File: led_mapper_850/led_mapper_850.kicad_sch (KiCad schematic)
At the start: 530 parts, among them J1 Conn_02x12_Top_Bottom

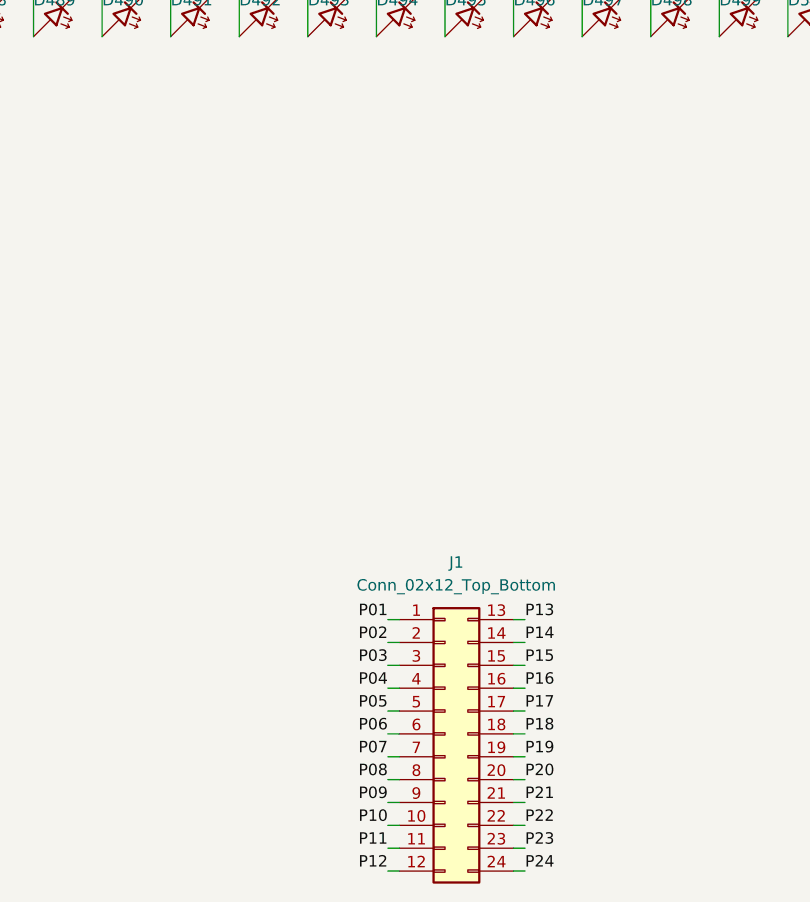
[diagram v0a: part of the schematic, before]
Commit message: lay out network from pcb positions
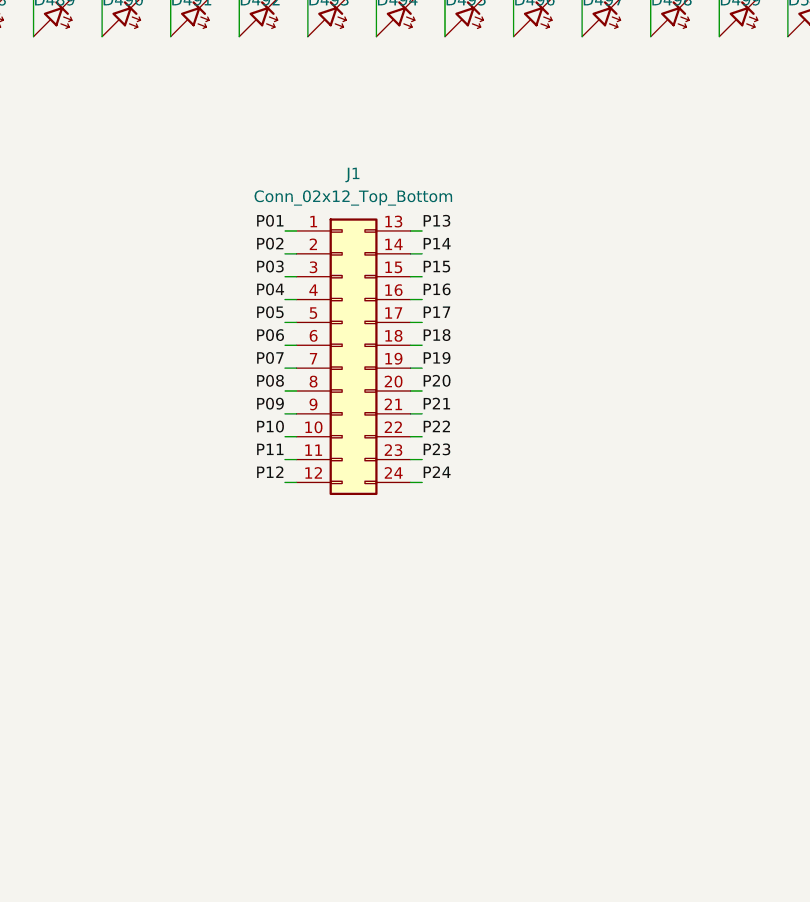
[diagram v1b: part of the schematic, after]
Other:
- moved on the sheet: J1
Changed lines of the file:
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@@
 	(wire
 		(pts
-			(xy 299.72 198.12) (xy 300.99 198.12)
+			(xy 288.29 154.94) (xy 289.56 154.94)
 		)
 		(stroke
@@
 	(wire
 		(pts
-			(xy 314.96 175.26) (xy 313.69 175.26)
+			(xy 303.53 132.08) (xy 302.26 132.08)
 		)
 		(stroke
@@
 	(wire
 		(pts
-			(xy 299.72 172.72) (xy 300.99 172.72)
+			(xy 288.29 129.54) (xy 289.56 129.54)
 		)
 		(stroke
@@
 	(wire
 		(pts
-			(xy 299.72 200.66) (xy 300.99 200.66)
+			(xy 288.29 157.48) (xy 289.56 157.48)
 		)
 		(stroke
@@
 	(wire
 		(pts
-			(xy 314.96 198.12) (xy 313.69 198.12)
+			(xy 303.53 154.94) (xy 302.26 154.94)
 		)
 		(stroke
@@
 	(wire
 		(pts
-			(xy 299.72 185.42) (xy 300.99 185.42)
+			(xy 288.29 142.24) (xy 289.56 142.24)
 		)
 		(stroke
@@
 	(wire
 		(pts
-			(xy 314.96 195.58) (xy 313.69 195.58)
+			(xy 303.53 152.4) (xy 302.26 152.4)
 		)
 		(stroke
@@
 	(wire
 		(pts
-			(xy 314.96 180.34) (xy 313.69 180.34)
+			(xy 303.53 137.16) (xy 302.26 137.16)
 		)
 		(stroke
@@
 	(wire
 		(pts
-			(xy 314.96 182.88) (xy 313.69 182.88)
+			(xy 303.53 139.7) (xy 302.26 139.7)
 		)
 		(stroke
@@
 	(wire
 		(pts
-			(xy 314.96 177.8) (xy 313.69 177.8)
+			(xy 303.53 134.62) (xy 302.26 134.62)
 		)
 		(stroke
@@
 	(wire
 		(pts
-			(xy 314.96 185.42) (xy 313.69 185.42)
+			(xy 303.53 142.24) (xy 302.26 142.24)
 		)
 		(stroke
@@
 	(wire
 		(pts
-			(xy 314.96 187.96) (xy 313.69 187.96)
+			(xy 303.53 144.78) (xy 302.26 144.78)
 		)
 		(stroke
@@
 	(wire
 		(pts
-			(xy 299.72 187.96) (xy 300.99 187.96)
+			(xy 288.29 144.78) (xy 289.56 144.78)
 		)
 		(stroke
@@
 	(wire
 		(pts
-			(xy 299.72 193.04) (xy 300.99 193.04)
+			(xy 288.29 149.86) (xy 289.56 149.86)
 		)
 		(stroke
@@
 	(wire
 		(pts
-			(xy 314.96 190.5) (xy 313.69 190.5)
+			(xy 303.53 147.32) (xy 302.26 147.32)
 		)
 		(stroke
@@
 	(wire
 		(pts
-			(xy 299.72 182.88) (xy 300.99 182.88)
+			(xy 288.29 139.7) (xy 289.56 139.7)
 		)
 		(stroke
@@
 	(wire
 		(pts
-			(xy 314.96 200.66) (xy 313.69 200.66)
+			(xy 303.53 157.48) (xy 302.26 157.48)
 		)
 		(stroke
@@
 	(wire
 		(pts
-			(xy 314.96 172.72) (xy 313.69 172.72)
+			(xy 303.53 129.54) (xy 302.26 129.54)
 		)
 		(stroke
@@
 	(wire
 		(pts
-			(xy 299.72 175.26) (xy 300.99 175.26)
+			(xy 288.29 132.08) (xy 289.56 132.08)
 		)
 		(stroke
@@
 	(wire
 		(pts
-			(xy 299.72 177.8) (xy 300.99 177.8)
+			(xy 288.29 134.62) (xy 289.56 134.62)
 		)
 		(stroke
@@
 	(wire
 		(pts
-			(xy 299.72 195.58) (xy 300.99 195.58)
+			(xy 288.29 152.4) (xy 289.56 152.4)
 		)
 		(stroke
@@
 	(wire
 		(pts
-			(xy 299.72 190.5) (xy 300.99 190.5)
+			(xy 288.29 147.32) (xy 289.56 147.32)
 		)
 		(stroke
@@
 	(wire
 		(pts
-			(xy 314.96 193.04) (xy 313.69 193.04)
+			(xy 303.53 149.86) (xy 302.26 149.86)
 		)
 		(stroke
@@
 	(wire
 		(pts
-			(xy 299.72 180.34) (xy 300.99 180.34)
+			(xy 288.29 137.16) (xy 289.56 137.16)
 		)
 		(stroke
@@
 	)
 	(label "P20"
-		(at 314.96 190.5 0)
+		(at 303.53 147.32 0)
 		(effects
 			(font
@@
 	)
 	(label "P14"
-		(at 314.96 175.26 0)
+		(at 303.53 132.08 0)
 		(effects
 			(font
@@
 	)
 	(label "P18"
-		(at 314.96 185.42 0)
+		(at 303.53 142.24 0)
 		(effects
 			(font
@@
 	)
 	(label "P11"
-		(at 299.72 198.12 180)
+		(at 288.29 154.94 180)
 		(effects
 			(font
@@
 	)
 	(label "P17"
-		(at 314.96 182.88 0)
+		(at 303.53 139.7 0)
 		(effects
 			(font
@@
 	)
 	(label "P05"
-		(at 299.72 182.88 180)
+		(at 288.29 139.7 180)
 		(effects
 			(font
@@
 	)
 	(label "P07"
-		(at 299.72 187.96 180)
+		(at 288.29 144.78 180)
 		(effects
 			(font
@@
 	)
 	(label "P02"
-		(at 299.72 175.26 180)
+		(at 288.29 132.08 180)
 		(effects
 			(font
@@
 	)
 	(label "P21"
-		(at 314.96 193.04 0)
+		(at 303.53 149.86 0)
 		(effects
 			(font
@@
 	)
 	(label "P09"
-		(at 299.72 193.04 180)
+		(at 288.29 149.86 180)
 		(effects
 			(font
@@
 	)
 	(label "P08"
-		(at 299.72 190.5 180)
+		(at 288.29 147.32 180)
 		(effects
 			(font
@@
 	)
 	(label "P13"
-		(at 314.96 172.72 0)
+		(at 303.53 129.54 0)
 		(effects
 			(font
@@
 	)
 	(label "P23"
-		(at 314.96 198.12 0)
+		(at 303.53 154.94 0)
 		(effects
 			(font
@@
 	)
 	(label "P10"
-		(at 299.72 195.58 180)
+		(at 288.29 152.4 180)
 		(effects
 			(font
@@
 	)
 	(label "P16"
-		(at 314.96 180.34 0)
+		(at 303.53 137.16 0)
 		(effects
 			(font
@@
 	)
 	(label "P15"
-		(at 314.96 177.8 0)
+		(at 303.53 134.62 0)
 		(effects
 			(font
@@
 	)
 	(label "P06"
-		(at 299.72 185.42 180)
+		(at 288.29 142.24 180)
 		(effects
 			(font
@@
 	)
 	(label "P12"
-		(at 299.72 200.66 180)
+		(at 288.29 157.48 180)
 		(effects
 			(font
@@
 	)
 	(label "P01"
-		(at 299.72 172.72 180)
+		(at 288.29 129.54 180)
 		(effects
 			(font
@@
 	)
 	(label "P24"
-		(at 314.96 200.66 0)
+		(at 303.53 157.48 0)
 		(effects
 			(font
@@
 	)
 	(label "P04"
-		(at 299.72 180.34 180)
+		(at 288.29 137.16 180)
 		(effects
 			(font
@@
 	)
 	(label "P19"
-		(at 314.96 187.96 0)
+		(at 303.53 144.78 0)
 		(effects
 			(font
@@
 	)
 	(label "P03"
-		(at 299.72 177.8 180)
+		(at 288.29 134.62 180)
 		(effects
 			(font
@@
 	)
 	(label "P22"
-		(at 314.96 195.58 0)
+		(at 303.53 152.4 0)
 		(effects
 			(font
@@
 	(symbol
 		(lib_id "Connector_Generic:Conn_02x12_Top_Bottom")
-		(at 306.07 185.42 0)
+		(at 294.64 142.24 0)
 		(unit 1)
 		(exclude_from_sim no)
@@
 		(fields_autoplaced yes)
 		(property "Reference" "J1"
-			(at 307.34 166.37 0)
+			(at 295.91 123.19 0)
 			(effects
 				(font
@@
 		)
 		(property "Value" "Conn_02x12_Top_Bottom"
-			(at 307.34 168.91 0)
+			(at 295.91 125.73 0)
 			(effects
 				(font
@@
 		)
 		(property "Footprint" "ccatlib:PinSocket_2x12_P2.54mm_Vertical_SMD_custom"
-			(at 306.07 185.42 0)
+			(at 294.64 142.24 0)
 			(effects
 				(font
@@
 		)
 		(property "Datasheet" "~"
-			(at 306.07 185.42 0)
+			(at 294.64 142.24 0)
 			(effects
 				(font
@@
 		)
 		(property "Description" "Generic connector, double row, 02x12, top/bottom pin numbering scheme (row 1: 1...pins_per_row, row2: pins_per_row+1 ... num_pins), script generated (kicad-library-utils/schlib/autogen/connector/)"
-			(at 306.07 185.42 0)
+			(at 294.64 142.24 0)
 			(effects
 				(font

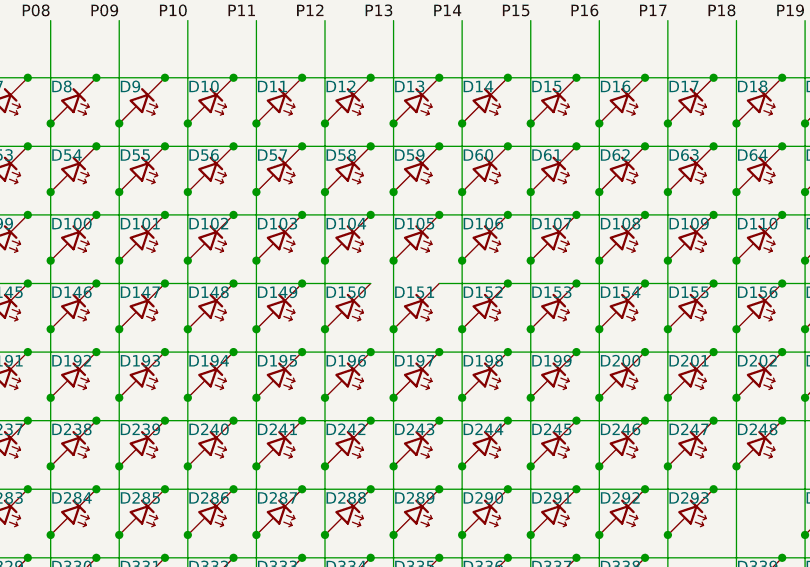
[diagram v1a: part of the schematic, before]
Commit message: fix wire disconnect
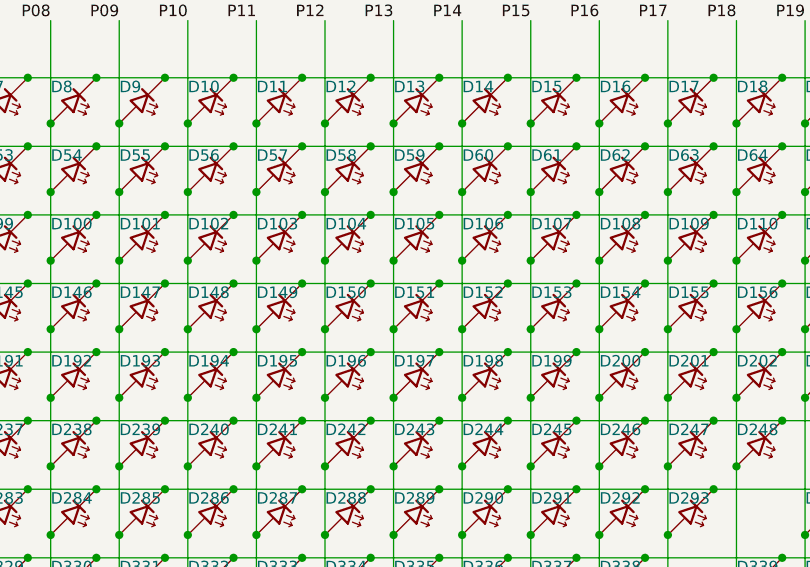
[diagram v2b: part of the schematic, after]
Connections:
- net P21: now also D151.1 (K), D152.1 (K), D153.1 (K), D154.1 (K), D155.1 (K), D156.1 (K), D157.1 (K), D158.1 (K), D159.1 (K), D160.1 (K), D161.1 (K)
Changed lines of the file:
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@@
 	)
 	(junction
+		(at 113.03 49.53)
+		(diameter 0)
+		(color 0 0 0 0)
+	)
+	(junction
 		(at 364.49 49.53)
 		(diameter 0)
@@
 	)
 	(junction
+		(at 120.65 49.53)
+		(diameter 0)
+		(color 0 0 0 0)
+	)
+	(junction
 		(at 237.49 100.33)
 		(diameter 0)
@@
 		)
 		(stroke
+			(width 0)
+			(type default)
+		)
+	)
+	(wire
+		(pts
+			(xy 113.03 49.53) (xy 120.65 49.53)
+		)
+		(stroke

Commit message: split into four networks
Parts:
- removed D1, D10, D100, D101, D102, D103, D104, D105, D106, D107, D108, D109, D11, D110, D111, D112, D113, D114, D115, D116, D117, D118, D119, D12, D120, D121, D122, D123, D124, D125, D126, D127, D128, D129, D13, D130, D131, D132, D133, D134, D135, D136, D137, D138, D139, D14, D140, D141, D142, D143, D144, D145, D146, D147, D148, D149, D15, D150, D151, D152, D153, D154, D155, D156, D157, D158, D159, D16, D160, D161, D162, D163, D164, D165, D166, D167, D168, D169, D17, D170, D171, D172, D173, D174, D175, D176, D177, D178, D179, D18, D180, D181, D182, D183, D184, D185, D186, D187, D188, D189, D19, D190, D191, D192, D193, D194, D195, D196, D197, D198, D199, D2, D20, D200, D201, D202, D203, D204, D205, D206, D207, D208, D209, D21, D210, D211, D212, D213, D214, D215, D216, D217, D218, D219, D22, D220, D221, D222, D223, D224, D225, D226, D227, D228, D229, D23, D230, D231, D232, D233, D234, D235, D236, D237, D238, D239, D24, D240, D241, D242, D243, D244, D245, D246, D247, D248, D249, D25, D250, D251, D252, D253, D254, D255, D256, D257, D258, D259, D26, D260, D261, D262, D263, D264, D265, D266, D267, D268, D269, D27, D270, D271, D272, D273, D274, D275, D276, D277, D278, D279, D28, D280, D281, D282, D283, D284, D285, D286, D287, D288, D289, D29, D290, D291, D292, D293, D294, D295, D296, D297, D298, D299, D3, D30, D300, D301, D302, D303, D304, D305, D306, D307, D308, D309, D31, D310, D311, D312, D313, D314, D315, D316, D317, D318, D319, D32, D320, D321, D322, D323, D324, D325, D326, D327, D328, D329, D33, D330, D331, D332, D333, D334, D335, D336, D337, D338, D339, D34, D340, D341, D342, D343, D344, D345, D346, D347, D348, D349, D35, D350, D351, D352, D353, D354, D355, D356, D357, D358, D359, D36, D360, D361, D362, D363, D364, D365, D366, D367, D368, D369, D37, D370, D371, D372, D373, D374, D375, D376, D377, D378, D379, D38, D380, D381, D382, D383, D384, D385, D386, D387, D388, D389, D39, D390, D391, D392, D393, D394, D395, D396, D397, D398, D399, D4, D40, D400, D401, D402, D403, D404, D405, D406, D407, D408, D409, D41, D410, D411, D412, D413, D414, D415, D416, D417, D418, D419, D42, D420, D421, D422, D423, D424, D425, D426, D427, D428, D429, D43, D430, D431, D432, D433, D434, D435, D436, D437, D438, D439, D44, D440, D441, D442, D443, D444, D445, D446, D447, D448, D449, D45, D450, D451, D452, D453, D454, D455, D456, D457, D458, D459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: LED, LED_SMD:LED_0201_0603Metric, symbol Device:LED_45deg
- removed J1: Conn_02x12_Top_Bottom, ccatlib:PinSocket_2x12_P2.54mm_Vertical_SMD_custom, symbol Connector_Generic:Conn_02x12_Top_Bottom
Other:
- added sheet network1 (untitled.kicad_sch)
- added sheet network2 (untitled.kicad_sch)
- added sheet network3 (untitled.kicad_sch)
- added sheet network4 (untitled.kicad_sch)

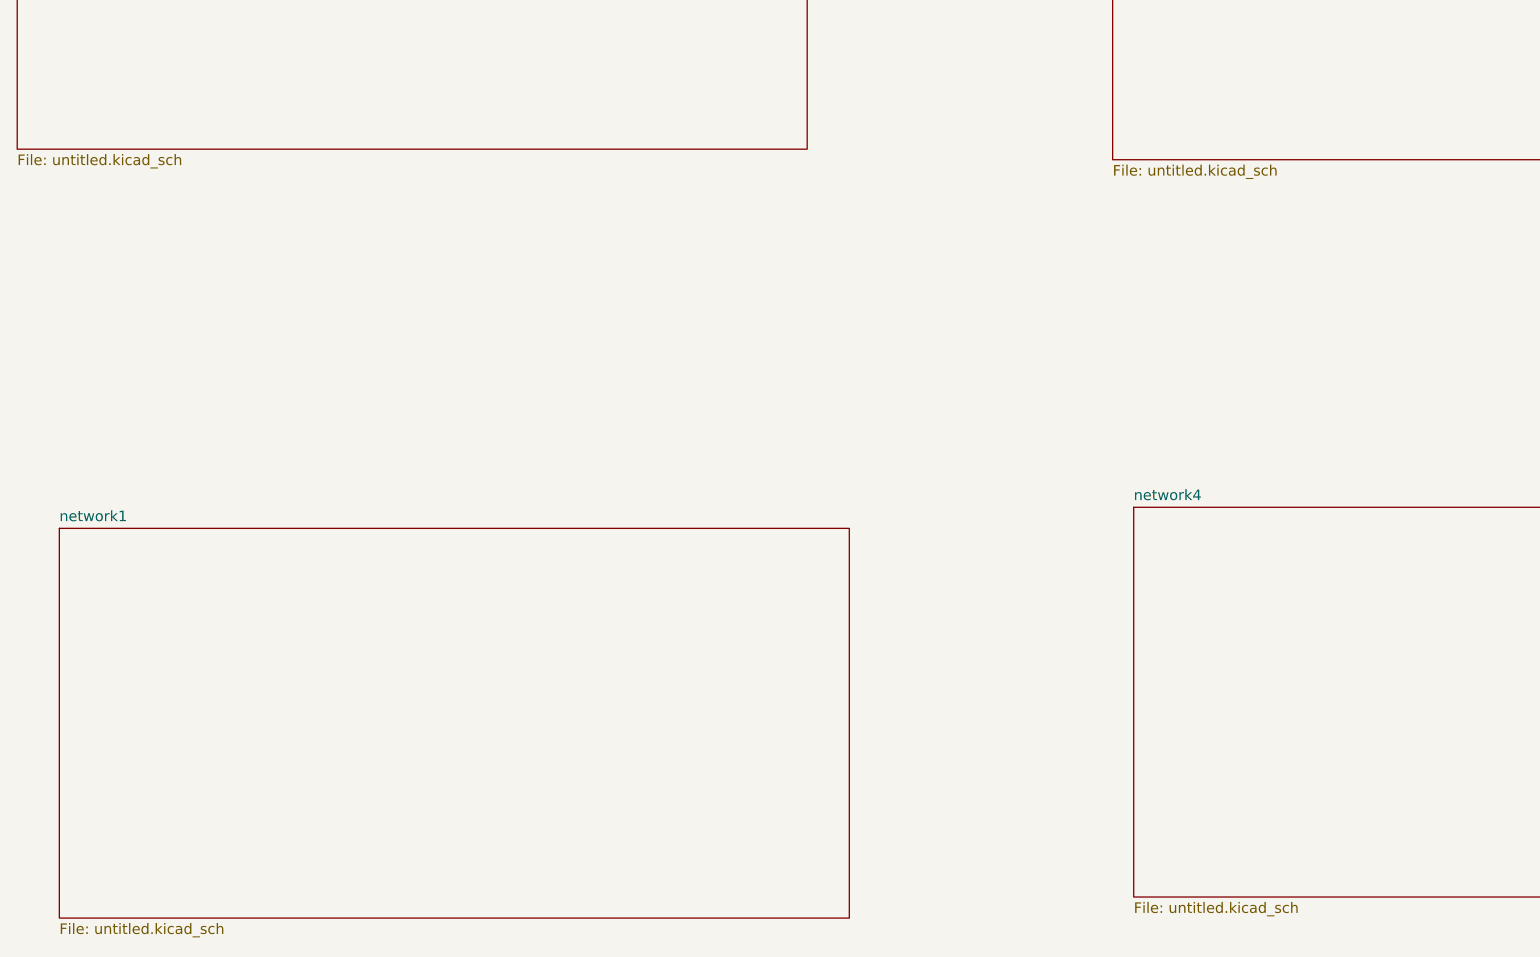
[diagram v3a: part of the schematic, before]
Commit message: rename single net schematic
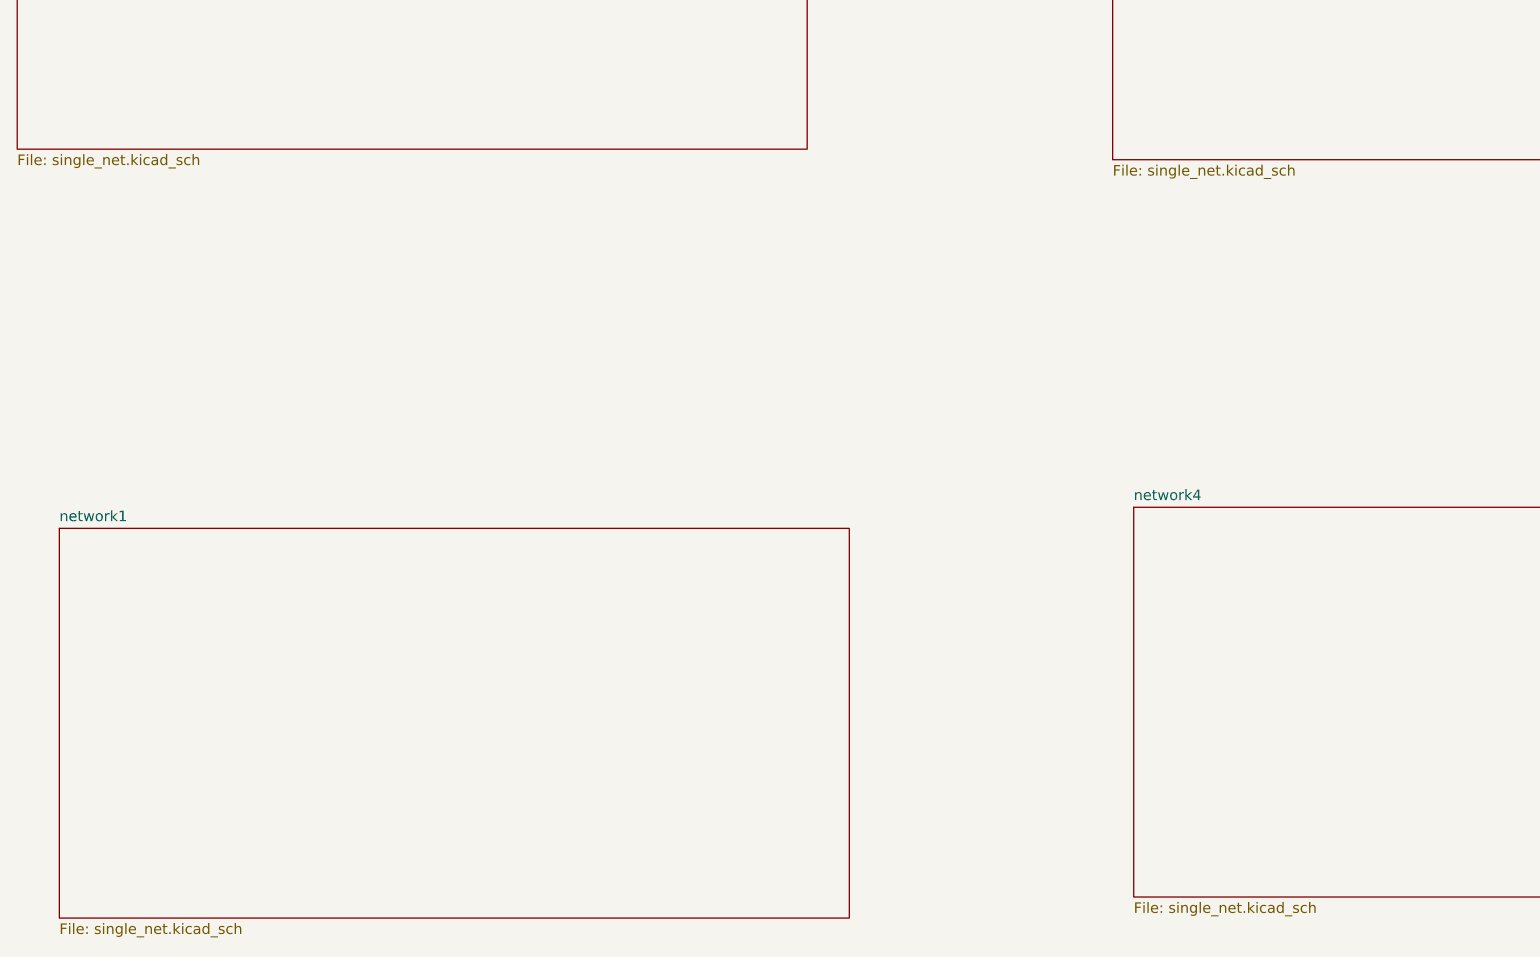
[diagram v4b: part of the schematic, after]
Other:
- sheet network1: file untitled.kicad_sch -> single_net.kicad_sch
- sheet network2: file untitled.kicad_sch -> single_net.kicad_sch
- sheet network3: file untitled.kicad_sch -> single_net.kicad_sch
- sheet network4: file untitled.kicad_sch -> single_net.kicad_sch
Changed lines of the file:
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@@
 			)
 		)
-		(property "Sheetfile" "untitled.kicad_sch"
+		(property "Sheetfile" "single_net.kicad_sch"
 			(at 29.21 164.4146 0)
 			(effects
@@
 			)
 		)
-		(property "Sheetfile" "untitled.kicad_sch"
+		(property "Sheetfile" "single_net.kicad_sch"
 			(at 156.21 72.9746 0)
 			(effects
@@
 			)
 		)
-		(property "Sheetfile" "untitled.kicad_sch"
+		(property "Sheetfile" "single_net.kicad_sch"
 			(at 158.75 161.8746 0)
 			(effects
@@
 			)
 		)
-		(property "Sheetfile" "untitled.kicad_sch"
+		(property "Sheetfile" "single_net.kicad_sch"
 			(at 24.13 71.7046 0)
 			(effects
